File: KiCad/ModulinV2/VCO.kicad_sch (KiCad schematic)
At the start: 107 parts, among them IC13 AS3340D, IC14 AS3340D, IC15 TL074HIDR, IC16 TL074HIDR, IC17 TL072HIDR, Q1 MMBFJ201, Q2 MMBFJ201, SW1 SW_SPDT_MSM

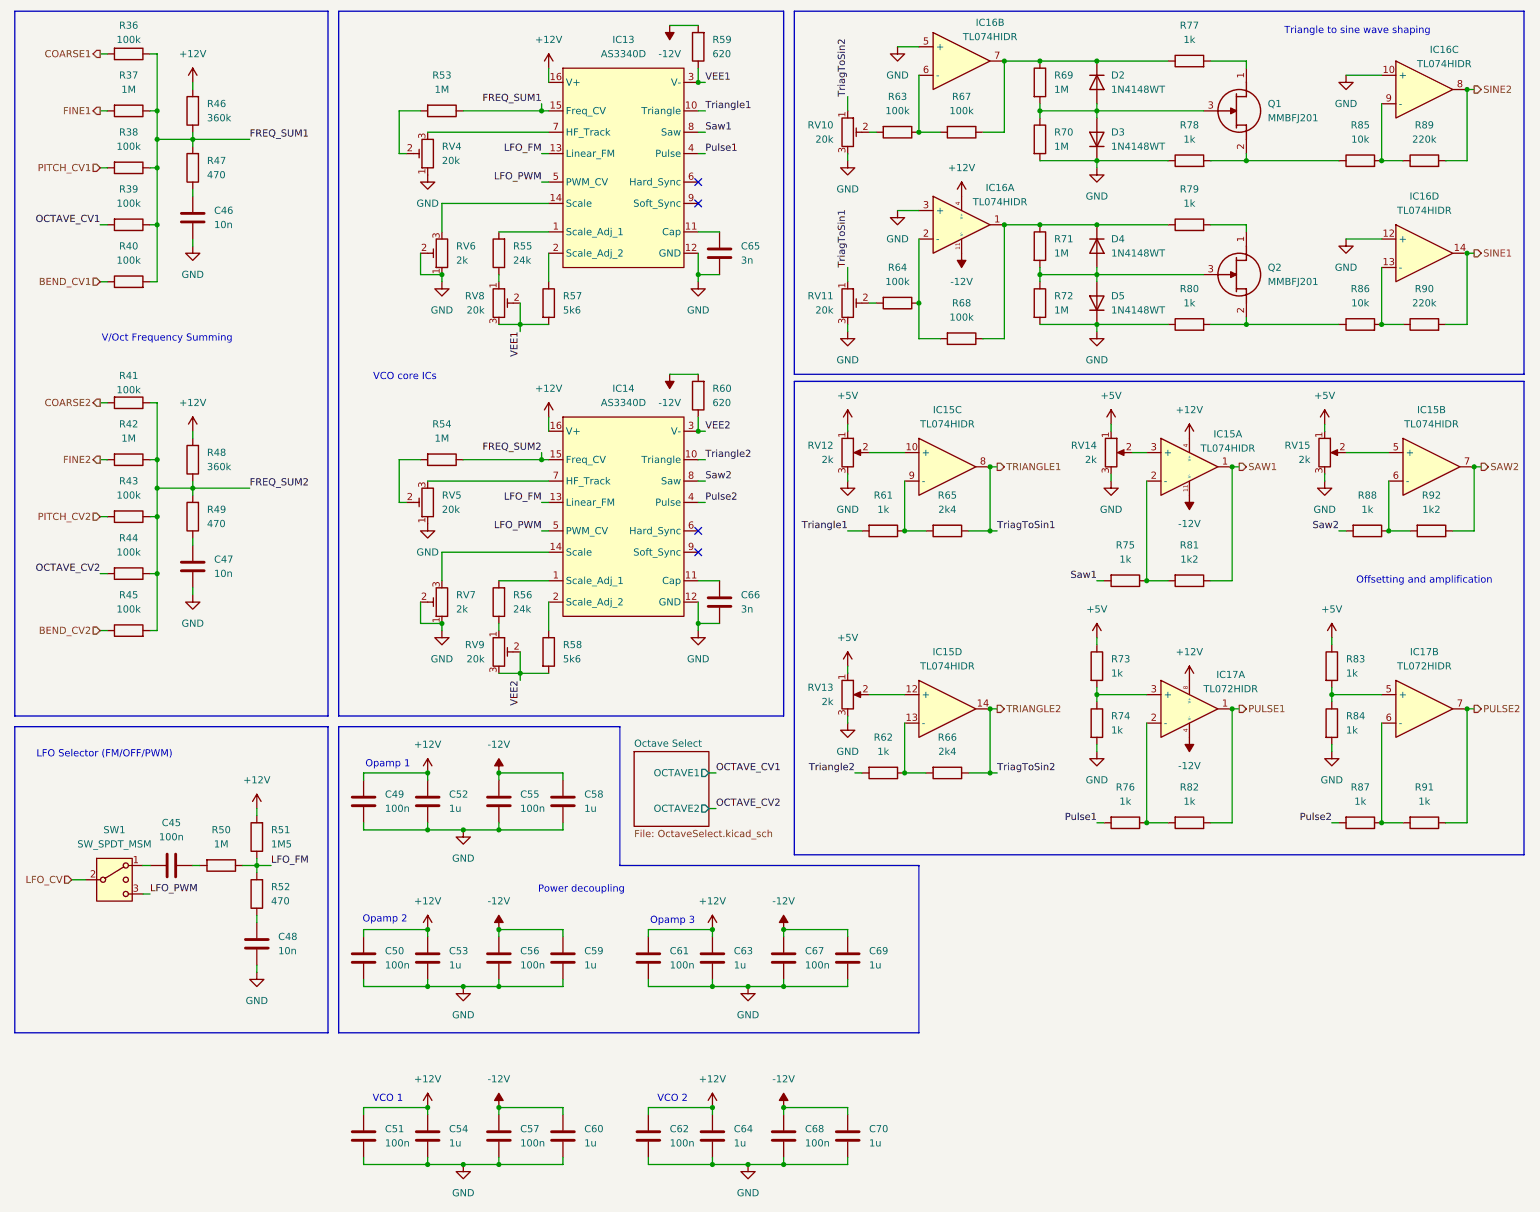
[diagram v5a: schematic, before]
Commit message: Layed out Interface and PWR components and started with MCU layout
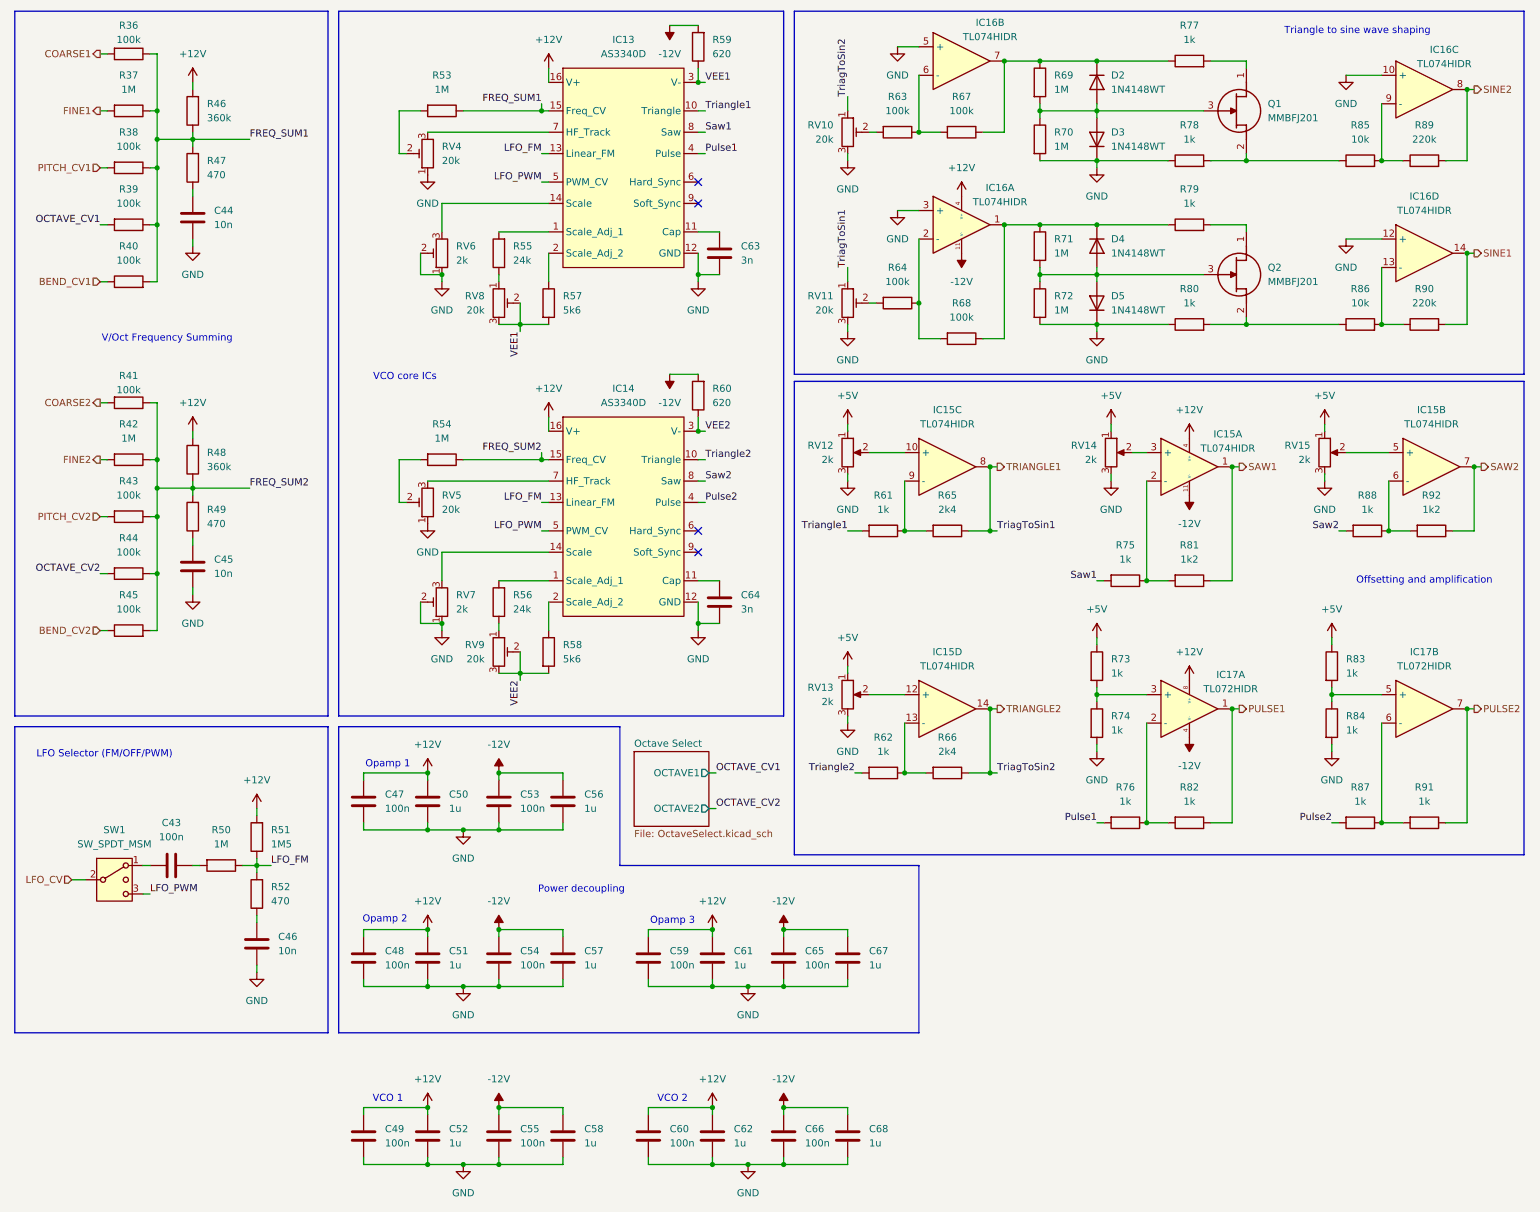
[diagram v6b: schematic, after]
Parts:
- renumbered C45 to C43, C46 to C44, C47 to C45, C48 to C46, C49 to C47, C50 to C48, C51 to C49, C52 to C50, C53 to C51, C54 to C52, C55 to C53, C56 to C54, C57 to C55, C58 to C56, C59 to C57, C60 to C58, C61 to C59, C62 to C60, C63 to C61, C64 to C62, C65 to C63, C66 to C64, C67 to C65, C68 to C66, C69 to C67, C70 to C68
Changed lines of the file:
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@@
 		(dnp no)
 		(fields_autoplaced yes)
-		(property "Reference" "C70"
+		(property "Reference" "C68"
 			(at 166.37 213.3599 0)
 			(effects
@@
 			(project "ModulinV2"
 				(path "/c6b34a57-3941-4b56-8b80-1848c7f41082/3ee27ced-353d-4052-9ca0-cd235d9ddb69"
-					(reference "C70")
+					(reference "C68")
 					(unit 1)
 				)
@@
 		(dnp no)
 		(fields_autoplaced yes)
-		(property "Reference" "C65"
+		(property "Reference" "C63"
 			(at 143.51 55.8799 0)
 			(effects
@@
 			(project ""
 				(path "/c6b34a57-3941-4b56-8b80-1848c7f41082/3ee27ced-353d-4052-9ca0-cd235d9ddb69"
-					(reference "C65")
+					(reference "C63")
 					(unit 1)
 				)
@@
 		(dnp no)
 		(fields_autoplaced yes)
-		(property "Reference" "C63"
+		(property "Reference" "C61"
 			(at 142.24 181.6099 0)
 			(effects
@@
 			(project "ModulinV2"
 				(path "/c6b34a57-3941-4b56-8b80-1848c7f41082/3ee27ced-353d-4052-9ca0-cd235d9ddb69"
-					(reference "C63")
+					(reference "C61")
 					(unit 1)
 				)
@@
 		(dnp no)
 		(fields_autoplaced yes)
-		(property "Reference" "C54"
+		(property "Reference" "C52"
 			(at 91.44 213.3599 0)
 			(effects
@@
 			(project "ModulinV2"
 				(path "/c6b34a57-3941-4b56-8b80-1848c7f41082/3ee27ced-353d-4052-9ca0-cd235d9ddb69"
-					(reference "C54")
+					(reference "C52")
 					(unit 1)
 				)
@@
 		(dnp no)
 		(fields_autoplaced yes)
-		(property "Reference" "C56"
+		(property "Reference" "C54"
 			(at 104.14 181.6099 0)
 			(effects
@@
 			(project "ModulinV2"
 				(path "/c6b34a57-3941-4b56-8b80-1848c7f41082/3ee27ced-353d-4052-9ca0-cd235d9ddb69"
-					(reference "C56")
+					(reference "C54")
 					(unit 1)
 				)
@@
 		(dnp no)
 		(fields_autoplaced yes)
-		(property "Reference" "C47"
+		(property "Reference" "C45"
 			(at 49.53 111.7599 0)
 			(effects
@@
 			(project "ModulinV2"
 				(path "/c6b34a57-3941-4b56-8b80-1848c7f41082/3ee27ced-353d-4052-9ca0-cd235d9ddb69"
-					(reference "C47")
+					(reference "C45")
 					(unit 1)
 				)
@@
 		(dnp no)
 		(fields_autoplaced yes)
-		(property "Reference" "C46"
+		(property "Reference" "C44"
 			(at 49.53 49.5299 0)
 			(effects
@@
 			(project "ModulinV2"
 				(path "/c6b34a57-3941-4b56-8b80-1848c7f41082/3ee27ced-353d-4052-9ca0-cd235d9ddb69"
-					(reference "C46")
+					(reference "C44")
 					(unit 1)
 				)
@@
 		(dnp no)
 		(fields_autoplaced yes)
-		(property "Reference" "C53"
+		(property "Reference" "C51"
 			(at 91.44 181.6099 0)
 			(effects
@@
 			(project "ModulinV2"
 				(path "/c6b34a57-3941-4b56-8b80-1848c7f41082/3ee27ced-353d-4052-9ca0-cd235d9ddb69"
-					(reference "C53")
+					(reference "C51")
 					(unit 1)
 				)
@@
 		(dnp no)
 		(fields_autoplaced yes)
-		(property "Reference" "C55"
+		(property "Reference" "C53"
 			(at 104.14 153.6699 0)
 			(effects
@@
 			(project "ModulinV2"
 				(path "/c6b34a57-3941-4b56-8b80-1848c7f41082/3ee27ced-353d-4052-9ca0-cd235d9ddb69"
-					(reference "C55")
+					(reference "C53")
 					(unit 1)
 				)
@@
 		(dnp no)
 		(fields_autoplaced yes)
-		(property "Reference" "C60"
+		(property "Reference" "C58"
 			(at 115.57 213.3599 0)
 			(effects
@@
 			(project "ModulinV2"
 				(path "/c6b34a57-3941-4b56-8b80-1848c7f41082/3ee27ced-353d-4052-9ca0-cd235d9ddb69"
-					(reference "C60")
+					(reference "C58")
 					(unit 1)
 				)
@@
 		(dnp no)
 		(fields_autoplaced yes)
-		(property "Reference" "C62"
+		(property "Reference" "C60"
 			(at 130.81 213.3599 0)
 			(effects
@@
 			(project "ModulinV2"
 				(path "/c6b34a57-3941-4b56-8b80-1848c7f41082/3ee27ced-353d-4052-9ca0-cd235d9ddb69"
-					(reference "C62")
+					(reference "C60")
 					(unit 1)
 				)
@@
 		(dnp no)
 		(fields_autoplaced yes)
-		(property "Reference" "C61"
+		(property "Reference" "C59"
 			(at 130.81 181.6099 0)
 			(effects
@@
 			(project "ModulinV2"
 				(path "/c6b34a57-3941-4b56-8b80-1848c7f41082/3ee27ced-353d-4052-9ca0-cd235d9ddb69"
-					(reference "C61")
+					(reference "C59")
 					(unit 1)
 				)
@@
 		(dnp no)
 		(fields_autoplaced yes)
-		(property "Reference" "C58"
+		(property "Reference" "C56"
 			(at 115.57 153.6699 0)
 			(effects
@@
 			(project "ModulinV2"
 				(path "/c6b34a57-3941-4b56-8b80-1848c7f41082/3ee27ced-353d-4052-9ca0-cd235d9ddb69"
-					(reference "C58")
+					(reference "C56")
 					(unit 1)
 				)
@@
 		(dnp no)
 		(fields_autoplaced yes)
-		(property "Reference" "C68"
+		(property "Reference" "C66"
 			(at 154.94 213.3599 0)
 			(effects
@@
 			(project "ModulinV2"
 				(path "/c6b34a57-3941-4b56-8b80-1848c7f41082/3ee27ced-353d-4052-9ca0-cd235d9ddb69"
-					(reference "C68")
+					(reference "C66")
 					(unit 1)
 				)
@@
 		(dnp no)
 		(fields_autoplaced yes)
-		(property "Reference" "C51"
+		(property "Reference" "C49"
 			(at 80.01 213.3599 0)
 			(effects
@@
 			(project "ModulinV2"
 				(path "/c6b34a57-3941-4b56-8b80-1848c7f41082/3ee27ced-353d-4052-9ca0-cd235d9ddb69"
-					(reference "C51")
+					(reference "C49")
 					(unit 1)
 				)
@@
 		(dnp no)
 		(fields_autoplaced yes)
-		(property "Reference" "C52"
+		(property "Reference" "C50"
 			(at 91.44 153.6699 0)
 			(effects
@@
 			(project "ModulinV2"
 				(path "/c6b34a57-3941-4b56-8b80-1848c7f41082/3ee27ced-353d-4052-9ca0-cd235d9ddb69"
-					(reference "C52")
+					(reference "C50")
 					(unit 1)
 				)
@@
 		(dnp no)
 		(fields_autoplaced yes)
-		(property "Reference" "C57"
+		(property "Reference" "C55"
 			(at 104.14 213.3599 0)
 			(effects
@@
 			(project "ModulinV2"
 				(path "/c6b34a57-3941-4b56-8b80-1848c7f41082/3ee27ced-353d-4052-9ca0-cd235d9ddb69"
-					(reference "C57")
+					(reference "C55")
 					(unit 1)
 				)
@@
 		(dnp no)
 		(fields_autoplaced yes)
-		(property "Reference" "C45"
+		(property "Reference" "C43"
 			(at 41.91 158.75 90)
 			(effects
@@
 			(project "ModulinV2"
 				(path "/c6b34a57-3941-4b56-8b80-1848c7f41082/3ee27ced-353d-4052-9ca0-cd235d9ddb69"
-					(reference "C45")
+					(reference "C43")
 					(unit 1)
 				)
@@
 		(dnp no)
 		(fields_autoplaced yes)
-		(property "Reference" "C67"
+		(property "Reference" "C65"
 			(at 154.94 181.6099 0)
 			(effects
@@
 			(project "ModulinV2"
 				(path "/c6b34a57-3941-4b56-8b80-1848c7f41082/3ee27ced-353d-4052-9ca0-cd235d9ddb69"
-					(reference "C67")
+					(reference "C65")
 					(unit 1)
 				)
@@
 		(dnp no)
 		(fields_autoplaced yes)
-		(property "Reference" "C50"
+		(property "Reference" "C48"
 			(at 80.01 181.6099 0)
 			(effects
@@
 			(project "ModulinV2"
 				(path "/c6b34a57-3941-4b56-8b80-1848c7f41082/3ee27ced-353d-4052-9ca0-cd235d9ddb69"
-					(reference "C50")
+					(reference "C48")
 					(unit 1)
 				)
@@
 		(dnp no)
 		(fields_autoplaced yes)
-		(property "Reference" "C49"
+		(property "Reference" "C47"
 			(at 80.01 153.6699 0)
 			(effects
@@
 			(project "ModulinV2"
 				(path "/c6b34a57-3941-4b56-8b80-1848c7f41082/3ee27ced-353d-4052-9ca0-cd235d9ddb69"
-					(reference "C49")
+					(reference "C47")
 					(unit 1)
 				)
@@
 		(dnp no)
 		(fields_autoplaced yes)
-		(property "Reference" "C69"
+		(property "Reference" "C67"
 			(at 166.37 181.6099 0)
 			(effects
@@
 			(project "ModulinV2"
 				(path "/c6b34a57-3941-4b56-8b80-1848c7f41082/3ee27ced-353d-4052-9ca0-cd235d9ddb69"
-					(reference "C69")
+					(reference "C67")
 					(unit 1)
 				)
@@
 		(dnp no)
 		(fields_autoplaced yes)
-		(property "Reference" "C66"
+		(property "Reference" "C64"
 			(at 143.51 118.1099 0)
 			(effects
@@
 			(project "ModulinV2"
 				(path "/c6b34a57-3941-4b56-8b80-1848c7f41082/3ee27ced-353d-4052-9ca0-cd235d9ddb69"
-					(reference "C66")
+					(reference "C64")
 					(unit 1)
 				)
@@
 		(dnp no)
 		(fields_autoplaced yes)
-		(property "Reference" "C48"
+		(property "Reference" "C46"
 			(at 60.96 179.0699 0)
 			(effects
@@
 			(project "ModulinV2"
 				(path "/c6b34a57-3941-4b56-8b80-1848c7f41082/3ee27ced-353d-4052-9ca0-cd235d9ddb69"
-					(reference "C48")
+					(reference "C46")
 					(unit 1)
 				)
@@
 		(dnp no)
 		(fields_autoplaced yes)
-		(property "Reference" "C64"
+		(property "Reference" "C62"
 			(at 142.24 213.3599 0)
 			(effects
@@
 			(project "ModulinV2"
 				(path "/c6b34a57-3941-4b56-8b80-1848c7f41082/3ee27ced-353d-4052-9ca0-cd235d9ddb69"
-					(reference "C64")
+					(reference "C62")
 					(unit 1)
 				)
@@
 		(dnp no)
 		(fields_autoplaced yes)
-		(property "Reference" "C59"
+		(property "Reference" "C57"
 			(at 115.57 181.6099 0)
 			(effects
@@
 			(project "ModulinV2"
 				(path "/c6b34a57-3941-4b56-8b80-1848c7f41082/3ee27ced-353d-4052-9ca0-cd235d9ddb69"
-					(reference "C59")
+					(reference "C57")
 					(unit 1)
 				)

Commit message: Completed tuning & mod wheel layouts
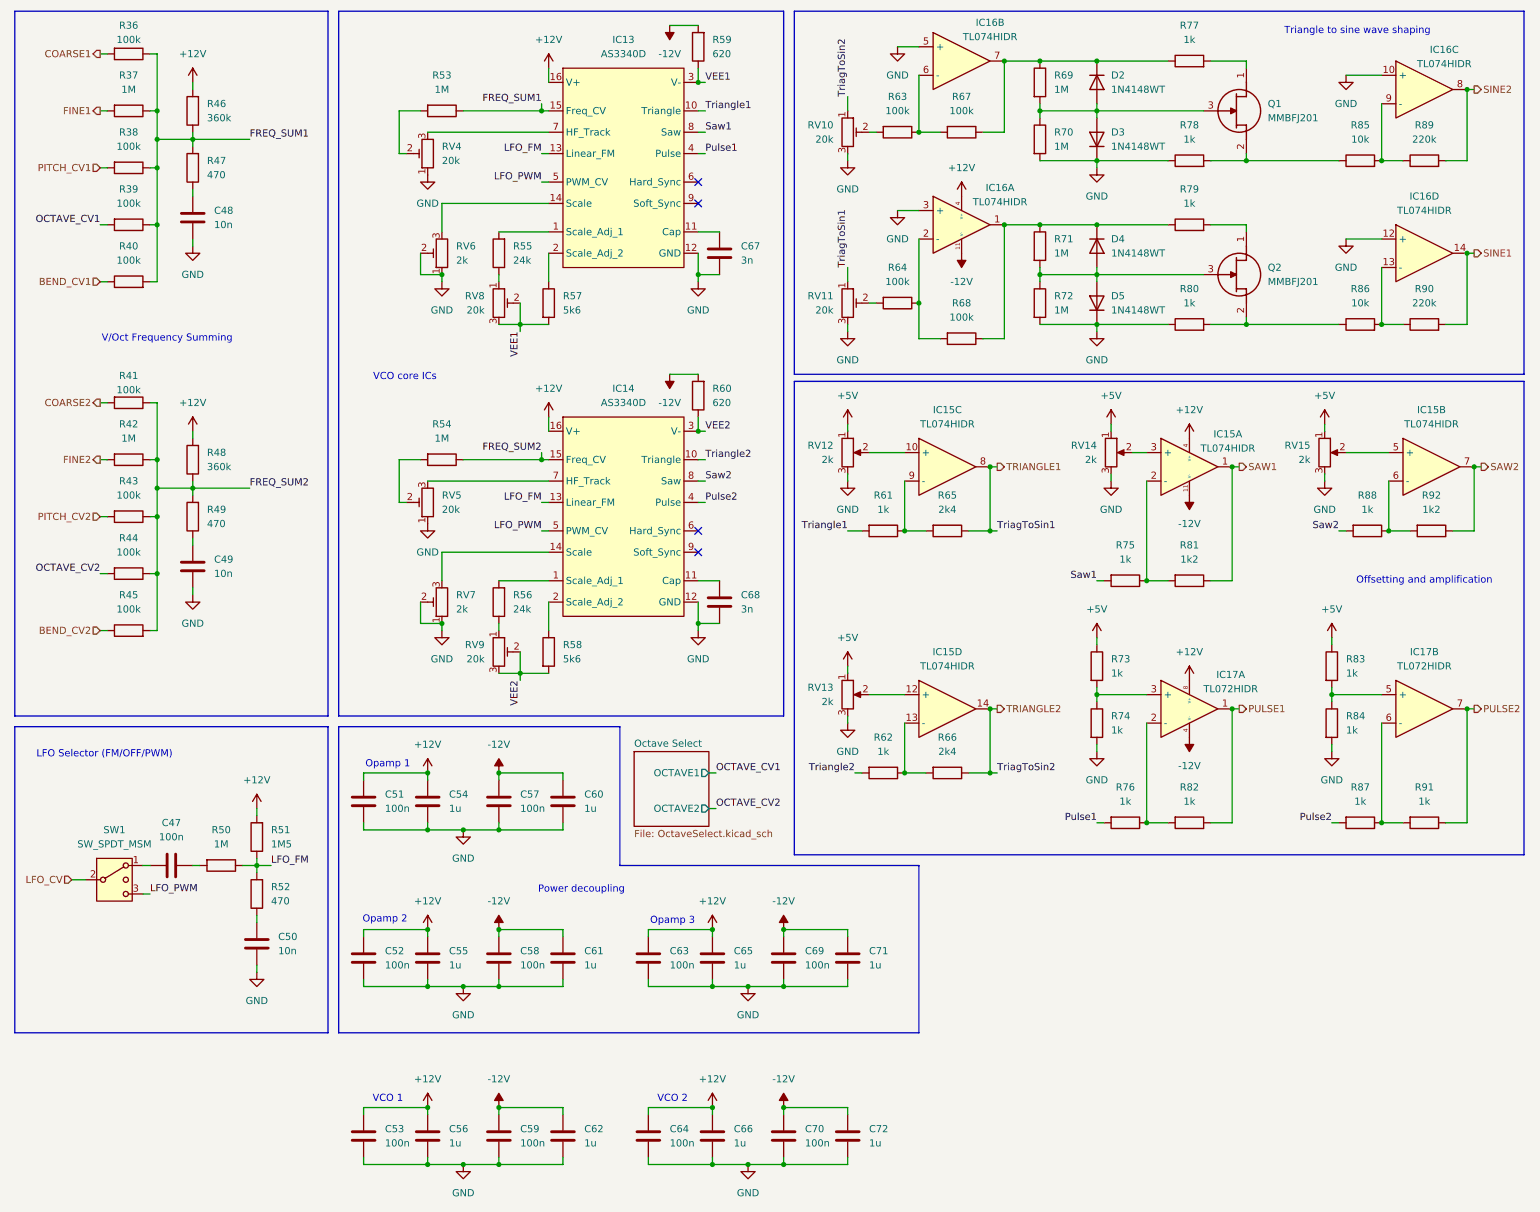
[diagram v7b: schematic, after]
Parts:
- renumbered C43 to C47, C44 to C48, C45 to C49, C46 to C50, C47 to C51, C48 to C52, C49 to C53, C50 to C54, C51 to C55, C52 to C56, C53 to C57, C54 to C58, C55 to C59, C56 to C60, C57 to C61, C58 to C62, C59 to C63, C60 to C64, C61 to C65, C62 to C66, C63 to C67, C64 to C68, C65 to C69, C66 to C70, C67 to C71, C68 to C72
